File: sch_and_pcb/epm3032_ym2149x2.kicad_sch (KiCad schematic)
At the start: 36 parts, among them Q1 BC847, U1 AMS1117-3.3, U2 NE5532, U3 YM2149, U4 YM2149, X1 zx-bus

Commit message: >> auto detect and division cpu clock 3.5/7 MHz for YM.
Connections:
- net d2: no longer D1.37 (io)
- new net int: D1.37 (io)
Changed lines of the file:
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@@
     (effects (font (size 1.27 1.27)) (justify left bottom))
   )
-  (label "d2" (at 157.48 53.34 180)
+  (label "int" (at 157.48 53.34 180)
     (effects (font (size 1.27 1.27)) (justify right bottom))
   )

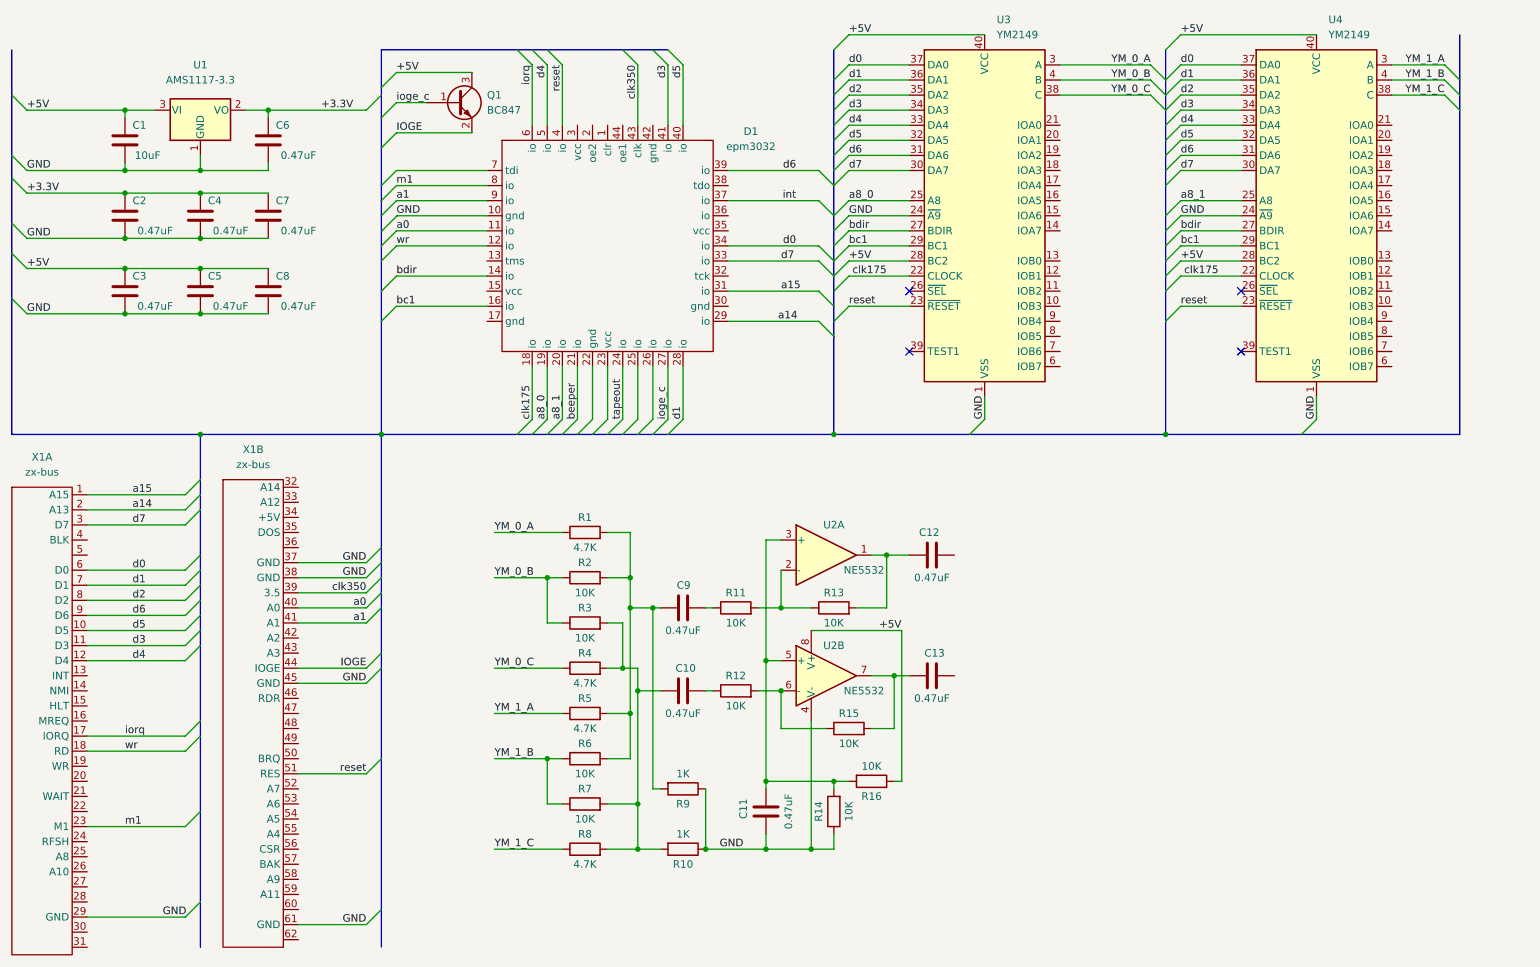
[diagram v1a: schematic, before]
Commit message: >> добавил сигнал dos, нужно тестировать.
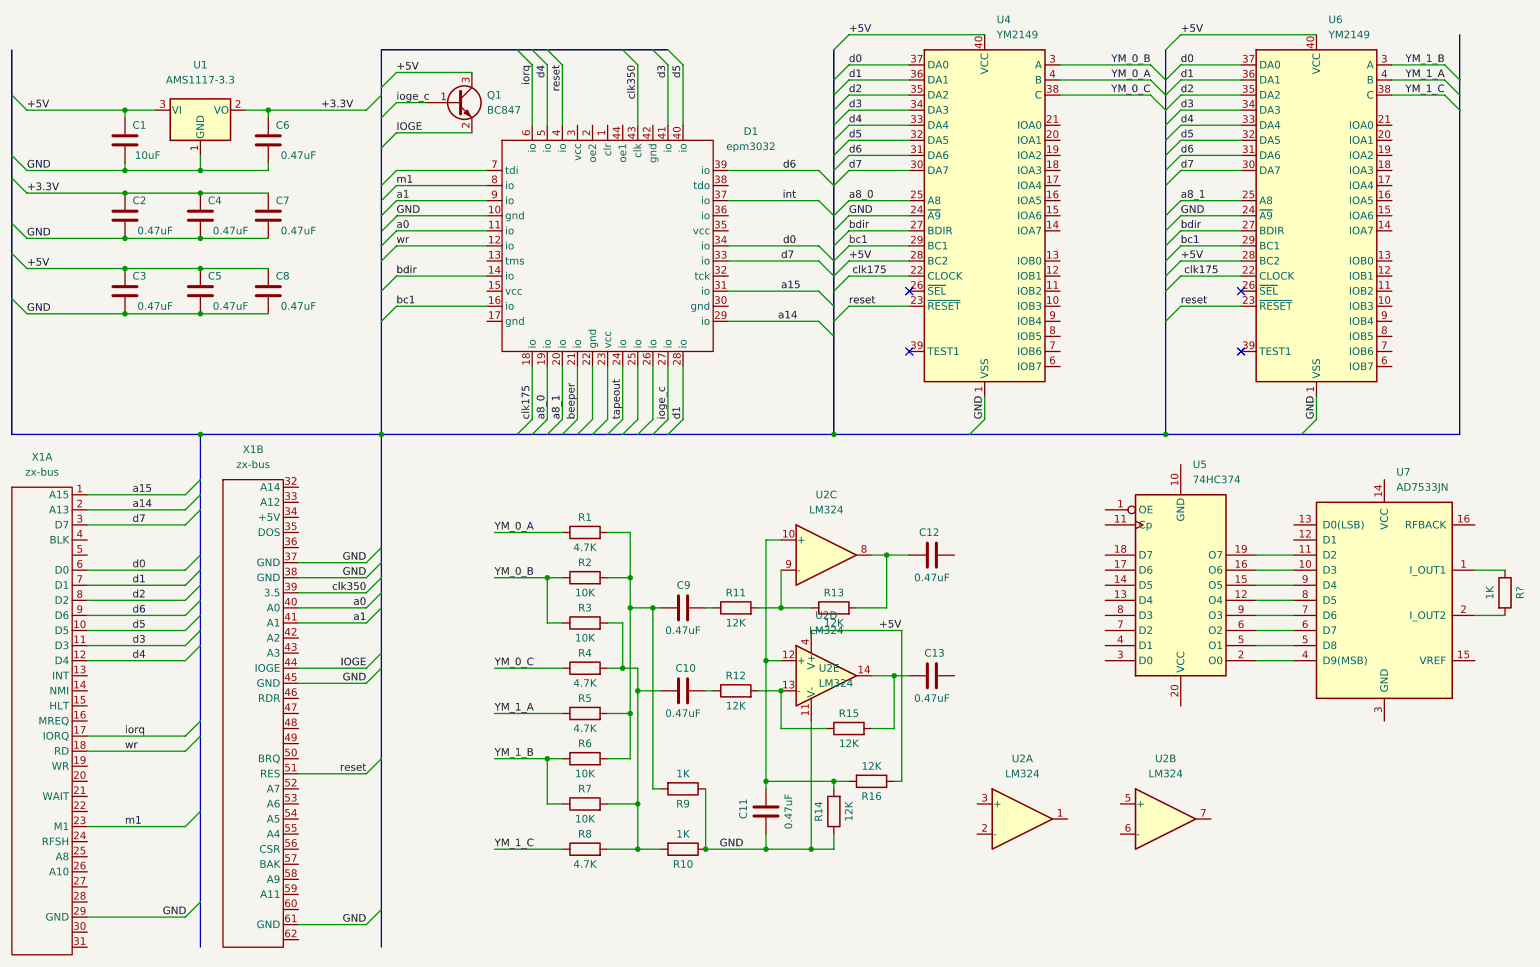
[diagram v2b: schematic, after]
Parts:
- removed U2: NE5532, Package_DIP:DIP-8_W7.62mm_Socket, symbol Amplifier_Operational:NE5532
- added R?: 1K, Resistor_SMD:R_0805_2012Metric_Pad1.20x1.40mm_HandSolder, symbol Device:R
- added U2: LM324, Package_DIP:DIP-14_W7.62mm, symbol Amplifier_Operational:LM324
- added U5: 74HC374, Package_DIP:DIP-20_W7.62mm, symbol 74xx:74HC374
- added U7: AD7533JN, Package_DIP:DIP-16_W7.62mm, symbol Analog_DAC:AD7533JN
- R11, R12, R13, R14, R15, R16: value 10K -> 12K
- renumbered U3 to U4, U4 to U6
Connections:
- net +5V: now also U2.4 (V+)
- net GND: now also U2.11 (V-)
- net YM_0_A: now also U4.4 (B); no longer U4.3 (A)
- net YM_0_B: now also U4.3 (A); no longer U4.4 (B)
- net YM_1_A: now also U6.4 (B); no longer U6.3 (A)
- net YM_1_B: now also U6.3 (A); no longer U6.4 (B)
- net at R12.2, R15.1: now also U2.13 (-)
- net at C11.1, R14.2, R16.2: now also U2.10 (+), U2.12 (+)
- net at C13.2, R15.2: now also U2.14
- net at R11.2, R13.1: now also U2.9 (-)
- net at C12.1, R13.2: now also U2.8
- new net: R?.1, U7.1 (I_OUT1)
- new net: R?.2, U7.2 (I_OUT2)
- new net: U5.16 (O6), U7.10 (D3)
- new net: U5.19 (O7), U7.11 (D2)
- new net: U5.2 (O0), U7.4 (D9(MSB))
- new net: U5.5 (O1), U7.5 (D8)
- new net: U5.6 (O2), U7.6 (D7)
- new net: U5.9 (O3), U7.7 (D6)
- new net: U5.12 (O4), U7.8 (D5)
- new net: U5.15 (O5), U7.9 (D4)
